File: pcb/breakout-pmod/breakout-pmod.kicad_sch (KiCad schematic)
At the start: 13 parts, among them J1 FX18-120P-0.8SV20

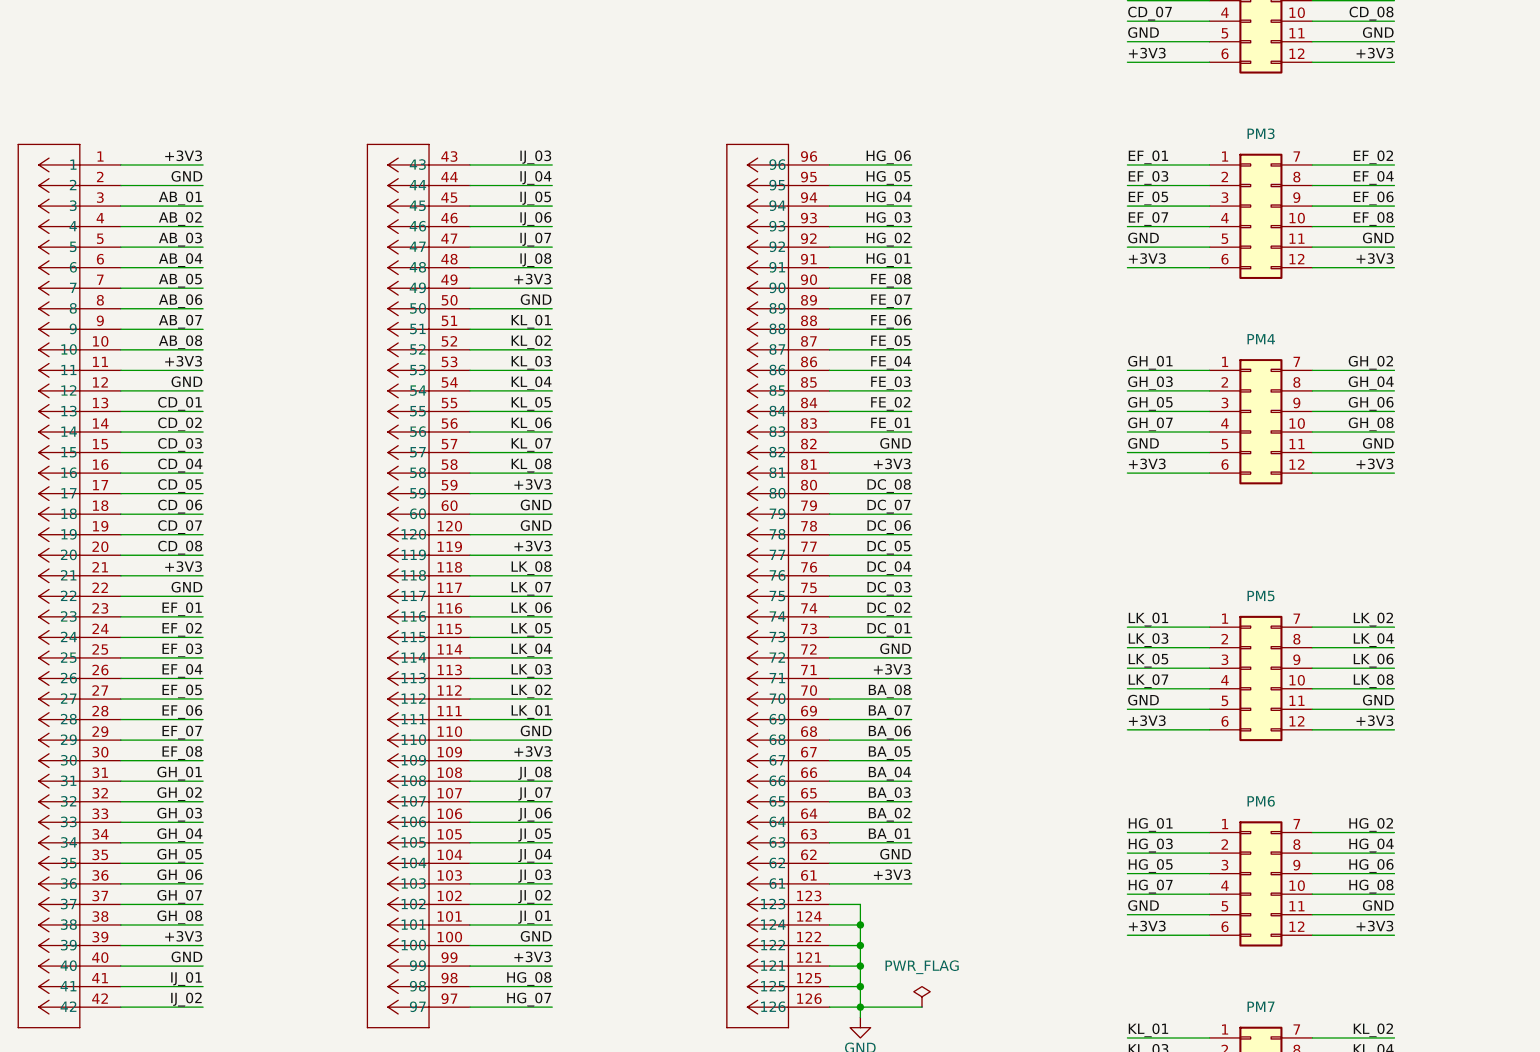
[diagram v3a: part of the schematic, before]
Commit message: [pmod] fix order of ef and gh pmod
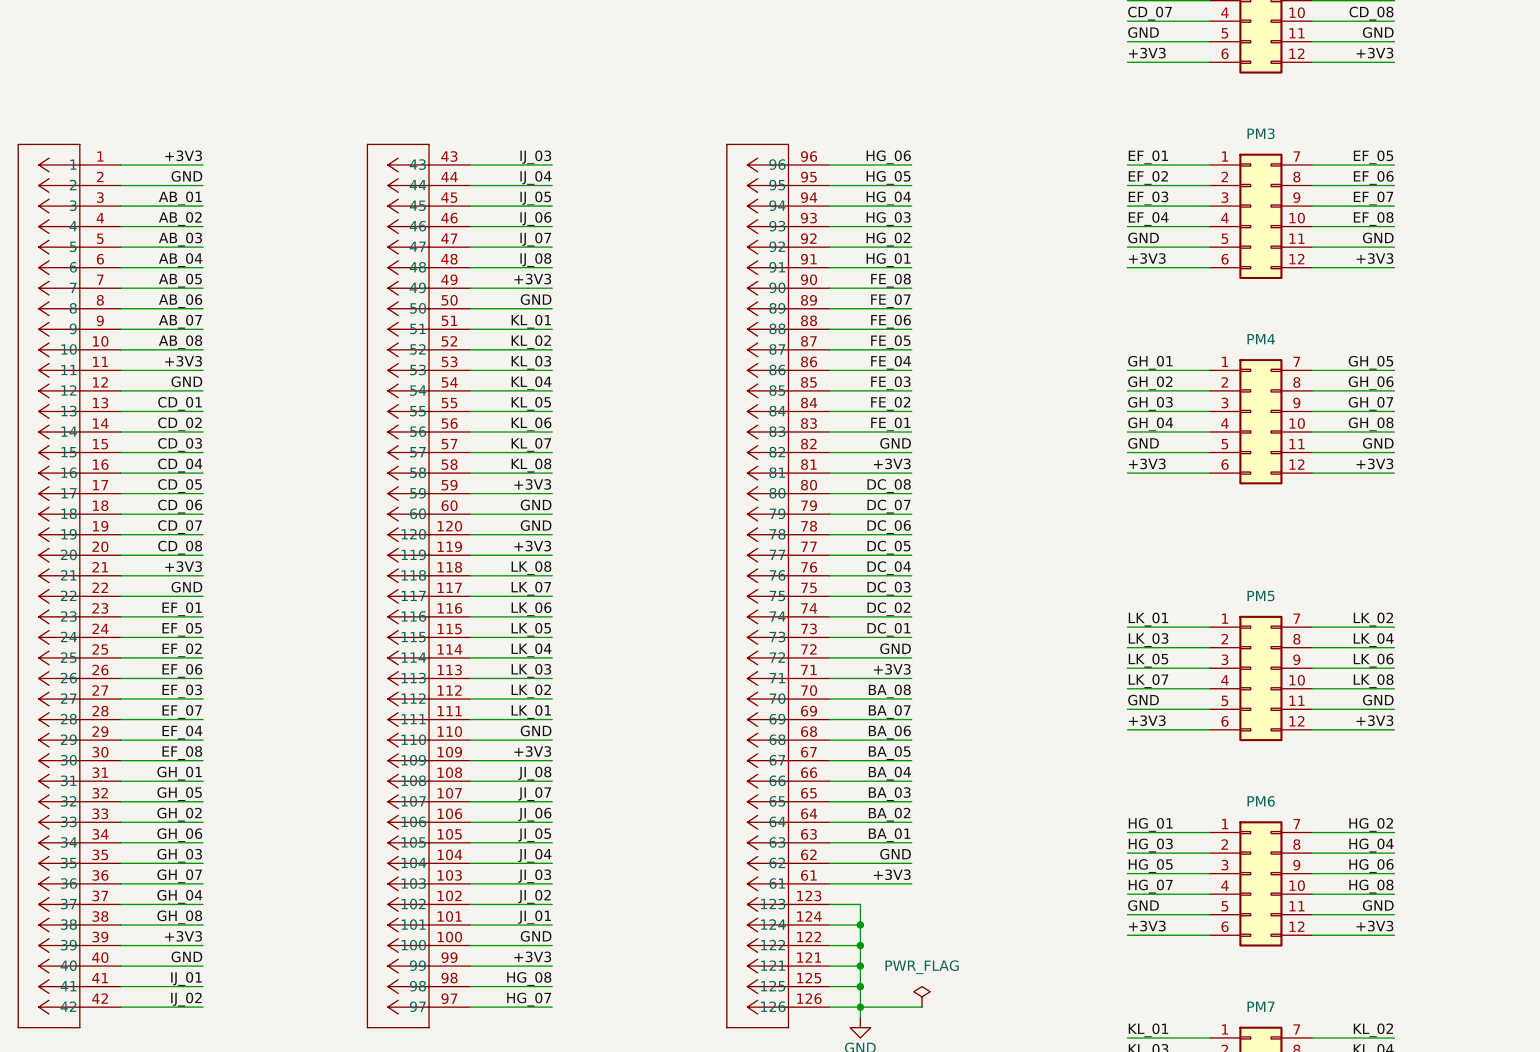
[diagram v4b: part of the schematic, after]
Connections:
- net EF_02: now also J1.25, PM3.2 (Pin_2); no longer J1.24, PM3.7 (Pin_7)
- net EF_03: now also J1.27, PM3.3 (Pin_3); no longer J1.25, PM3.2 (Pin_2)
- net EF_04: now also J1.29, PM3.4 (Pin_4); no longer J1.26, PM3.8 (Pin_8)
- net EF_05: now also J1.24, PM3.7 (Pin_7); no longer J1.27, PM3.3 (Pin_3)
- net EF_06: now also J1.26, PM3.8 (Pin_8); no longer J1.28, PM3.9 (Pin_9)
- net EF_07: now also J1.28, PM3.9 (Pin_9); no longer J1.29, PM3.4 (Pin_4)
- net GH_02: now also J1.33, PM4.2 (Pin_2); no longer J1.32, PM4.7 (Pin_7)
- net GH_03: now also J1.35, PM4.3 (Pin_3); no longer J1.33, PM4.2 (Pin_2)
- net GH_04: now also J1.37, PM4.4 (Pin_4); no longer J1.34, PM4.8 (Pin_8)
- net GH_05: now also J1.32, PM4.7 (Pin_7); no longer J1.35, PM4.3 (Pin_3)
- net GH_06: now also J1.34, PM4.8 (Pin_8); no longer J1.36, PM4.9 (Pin_9)
- net GH_07: now also J1.36, PM4.9 (Pin_9); no longer J1.37, PM4.4 (Pin_4)
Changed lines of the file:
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@@
 		)
 	)
-	(label "EF_05"
+	(label "EF_03"
 		(at 50.8 156.21 180)
 		(fields_autoplaced yes)
@@
 		)
 	)
-	(label "GH_05"
+	(label "GH_03"
 		(at 50.8 176.53 180)
 		(fields_autoplaced yes)
@@
 		)
 	)
-	(label "GH_03"
+	(label "GH_02"
 		(at 165.1 118.11 0)
 		(fields_autoplaced yes)
@@
 		)
 	)
-	(label "EF_07"
+	(label "EF_04"
 		(at 165.1 97.79 0)
 		(fields_autoplaced yes)
@@
 		)
 	)
-	(label "GH_07"
+	(label "GH_04"
 		(at 50.8 181.61 180)
 		(fields_autoplaced yes)
@@
 		)
 	)
-	(label "EF_05"
+	(label "EF_03"
 		(at 165.1 95.25 0)
 		(fields_autoplaced yes)
@@
 		)
 	)
-	(label "GH_06"
+	(label "GH_07"
 		(at 198.12 120.65 180)
 		(fields_autoplaced yes)
@@
 		)
 	)
-	(label "GH_02"
+	(label "GH_05"
 		(at 198.12 115.57 180)
 		(fields_autoplaced yes)
@@
 		)
 	)
-	(label "EF_02"
+	(label "EF_05"
 		(at 198.12 90.17 180)
 		(fields_autoplaced yes)
@@
 		)
 	)
-	(label "GH_05"
+	(label "GH_03"
 		(at 165.1 120.65 0)
 		(fields_autoplaced yes)
@@
 		)
 	)
-	(label "EF_07"
+	(label "EF_04"
 		(at 50.8 161.29 180)
 		(fields_autoplaced yes)
@@
 		)
 	)
-	(label "EF_03"
+	(label "EF_02"
 		(at 50.8 151.13 180)
 		(fields_autoplaced yes)
@@
 		)
 	)
-	(label "GH_06"
+	(label "GH_07"
 		(at 50.8 179.07 180)
 		(fields_autoplaced yes)
@@
 		)
 	)
-	(label "EF_02"
+	(label "EF_05"
 		(at 50.8 148.59 180)
 		(fields_autoplaced yes)
@@
 		)
 	)
-	(label "GH_07"
+	(label "GH_04"
 		(at 165.1 123.19 0)
 		(fields_autoplaced yes)
@@
 		)
 	)
-	(label "GH_04"
+	(label "GH_06"
 		(at 198.12 118.11 180)
 		(fields_autoplaced yes)
@@
 		)
 	)
-	(label "GH_04"
+	(label "GH_06"
 		(at 50.8 173.99 180)
 		(fields_autoplaced yes)
@@
 		)
 	)
-	(label "EF_03"
+	(label "EF_02"
 		(at 165.1 92.71 0)
 		(fields_autoplaced yes)
@@
 		)
 	)
-	(label "EF_04"
+	(label "EF_06"
 		(at 198.12 92.71 180)
 		(fields_autoplaced yes)
@@
 		)
 	)
-	(label "EF_06"
+	(label "EF_07"
 		(at 50.8 158.75 180)
 		(fields_autoplaced yes)
@@
 		)
 	)
-	(label "GH_03"
+	(label "GH_02"
 		(at 50.8 171.45 180)
 		(fields_autoplaced yes)
@@
 		)
 	)
-	(label "EF_04"
+	(label "EF_06"
 		(at 50.8 153.67 180)
 		(fields_autoplaced yes)
@@
 		)
 	)
-	(label "EF_06"
+	(label "EF_07"
 		(at 198.12 95.25 180)
 		(fields_autoplaced yes)
@@
 		)
 	)
-	(label "GH_02"
+	(label "GH_05"
 		(at 50.8 168.91 180)
 		(fields_autoplaced yes)

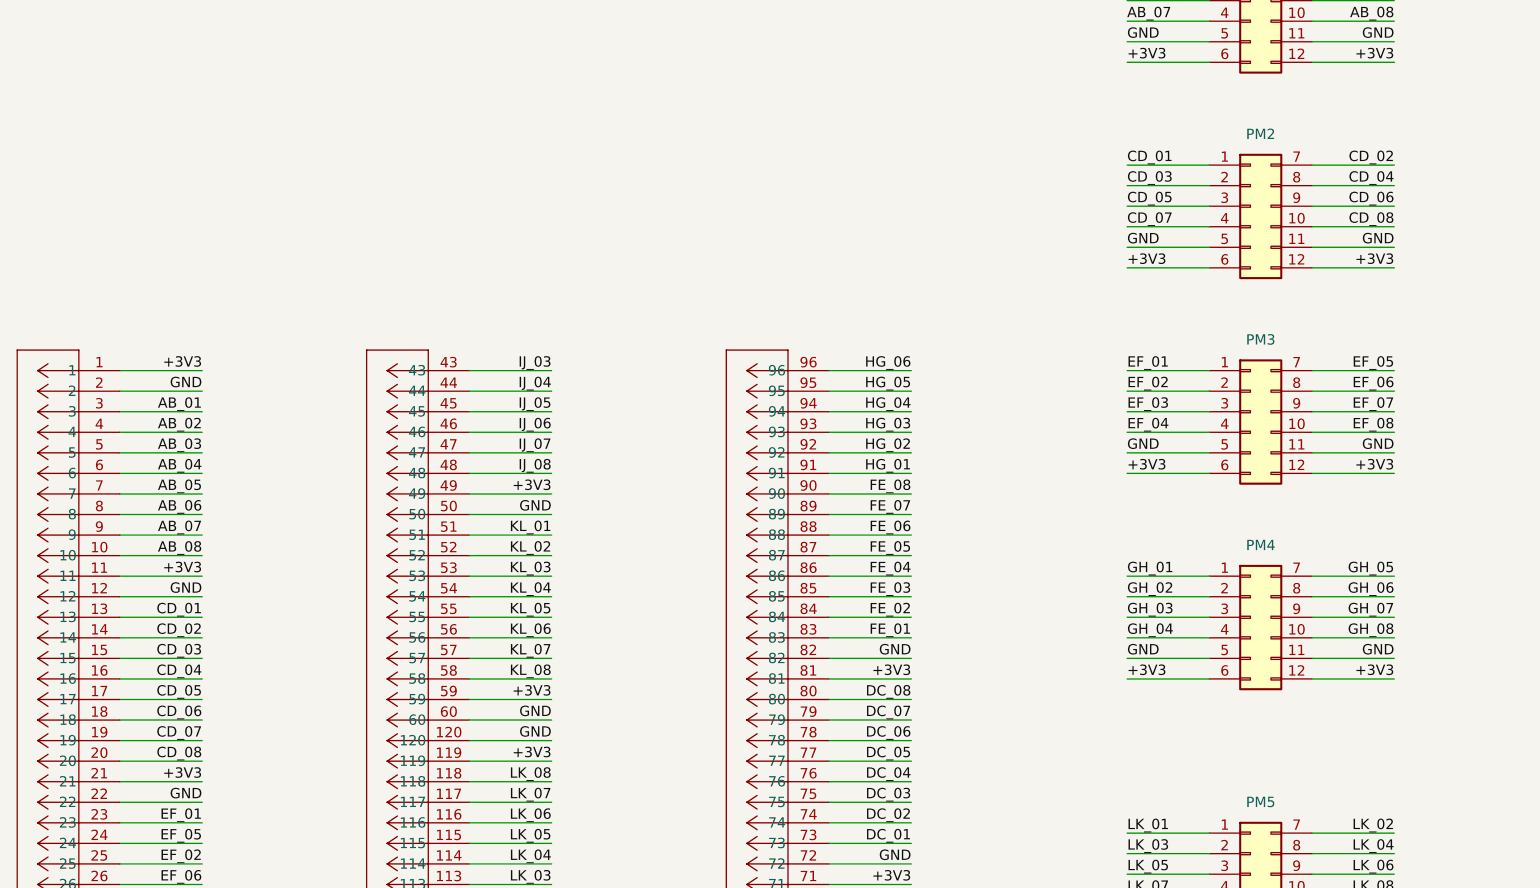
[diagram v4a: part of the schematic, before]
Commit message: [pmod] fix order of CD pmod
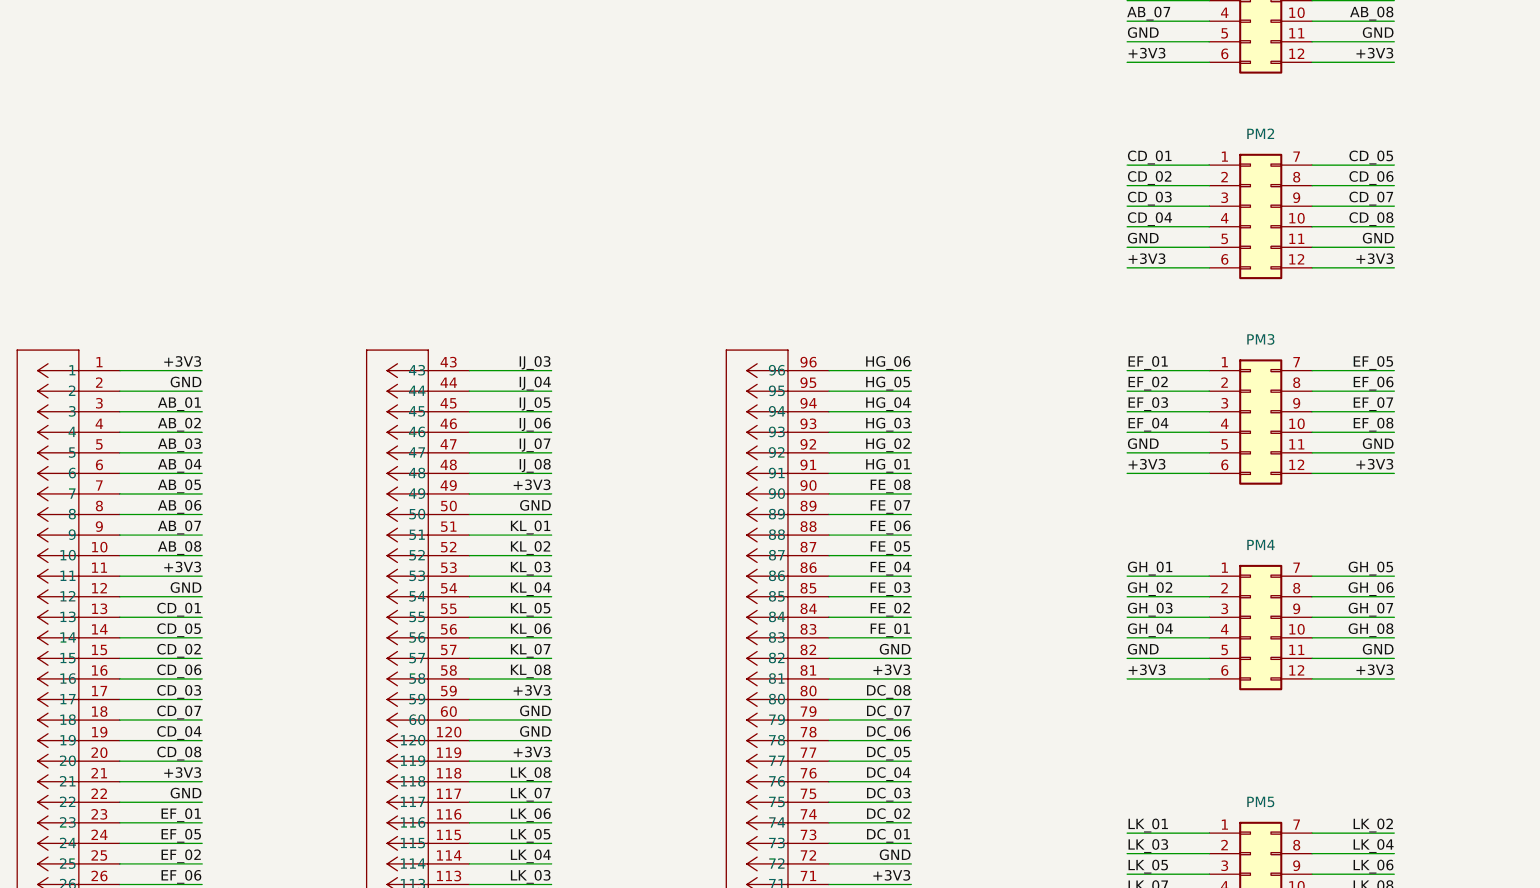
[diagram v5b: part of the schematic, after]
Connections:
- net CD_02: now also J1.15, PM2.2 (Pin_2); no longer J1.14, PM2.7 (Pin_7)
- net CD_03: now also J1.17, PM2.3 (Pin_3); no longer J1.15, PM2.2 (Pin_2)
- net CD_04: now also J1.19, PM2.4 (Pin_4); no longer J1.16, PM2.8 (Pin_8)
- net CD_05: now also J1.14, PM2.7 (Pin_7); no longer J1.17, PM2.3 (Pin_3)
- net CD_06: now also J1.16, PM2.8 (Pin_8); no longer J1.18, PM2.9 (Pin_9)
- net CD_07: now also J1.18, PM2.9 (Pin_9); no longer J1.19, PM2.4 (Pin_4)
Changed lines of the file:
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@@
 	)
 	(label "CD_06"
-		(at 198.12 69.85 180)
+		(at 198.12 67.31 180)
 		(fields_autoplaced yes)
 		(effects
@@
 	)
 	(label "CD_03"
-		(at 50.8 125.73 180)
+		(at 50.8 130.81 180)
 		(fields_autoplaced yes)
 		(effects
@@
 	)
 	(label "CD_04"
-		(at 198.12 67.31 180)
-		(fields_autoplaced yes)
-		(effects
-			(font
-				(size 1.27 1.27)
-			)
-			(justify right bottom)
+		(at 165.1 72.39 0)
+		(fields_autoplaced yes)
+		(effects
+			(font
+				(size 1.27 1.27)
+			)
+			(justify left bottom)
 		)
 	)
@@
 	)
 	(label "CD_05"
-		(at 165.1 69.85 0)
-		(fields_autoplaced yes)
-		(effects
-			(font
-				(size 1.27 1.27)
-			)
-			(justify left bottom)
+		(at 198.12 64.77 180)
+		(fields_autoplaced yes)
+		(effects
+			(font
+				(size 1.27 1.27)
+			)
+			(justify right bottom)
 		)
 	)
@@
 	)
 	(label "CD_07"
-		(at 165.1 72.39 0)
-		(fields_autoplaced yes)
-		(effects
-			(font
-				(size 1.27 1.27)
-			)
-			(justify left bottom)
+		(at 198.12 69.85 180)
+		(fields_autoplaced yes)
+		(effects
+			(font
+				(size 1.27 1.27)
+			)
+			(justify right bottom)
 		)
 	)
@@
 	)
 	(label "CD_05"
-		(at 50.8 130.81 180)
+		(at 50.8 123.19 180)
 		(fields_autoplaced yes)
 		(effects
@@
 	)
 	(label "CD_06"
-		(at 50.8 133.35 180)
+		(at 50.8 128.27 180)
 		(fields_autoplaced yes)
 		(effects
@@
 	)
 	(label "CD_04"
-		(at 50.8 128.27 180)
+		(at 50.8 135.89 180)
 		(fields_autoplaced yes)
 		(effects
@@
 	)
 	(label "CD_03"
-		(at 165.1 67.31 0)
+		(at 165.1 69.85 0)
 		(fields_autoplaced yes)
 		(effects
@@
 	)
 	(label "CD_02"
-		(at 198.12 64.77 180)
-		(fields_autoplaced yes)
-		(effects
-			(font
-				(size 1.27 1.27)
-			)
-			(justify right bottom)
+		(at 165.1 67.31 0)
+		(fields_autoplaced yes)
+		(effects
+			(font
+				(size 1.27 1.27)
+			)
+			(justify left bottom)
 		)
 	)
@@
 	)
 	(label "CD_07"
-		(at 50.8 135.89 180)
+		(at 50.8 133.35 180)
 		(fields_autoplaced yes)
 		(effects
@@
 	)
 	(label "CD_02"
-		(at 50.8 123.19 180)
-		(fields_autoplaced yes)
-		(effects
+		(at 50.8 125.73 180)
+		(fields_autoplaced yes)
+		(effects
